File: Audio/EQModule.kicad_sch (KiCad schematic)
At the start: 59 parts, among them J6 AUX_IN, J7 V_IN, J8 AUX_OUT, U2 NJM4558, U3 NJM4558, U4 NJM4558

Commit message: AudioCaseのリレー・EQネット整理と分割Gerberを再生成する。
Controllでアンプ別リレーネットを分離し、EQのバッファ入力をL/R_BUFF_INに改名。4枚分割PCBと発注用Gerberを更新し、RVパネルKiKit矩形とmacOS向けツール探索も修正。

Co-authored-by: Cursor <cursoragent@cursor.com>
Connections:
- net L_IN: no longer C20.1, C21.1, R16.1, U2.3 (+)
- net R_IN: no longer C18.1, C19.1, R15.1, U2.5 (+)
- new net L_BUFF_IN: C20.1, C21.1, R16.1, U2.3 (+)
- new net R_BUFF_IN: C18.1, C19.1, R15.1, U2.5 (+)
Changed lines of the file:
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@@
 		)
 	)
-	(label "L_IN"
+	(label "L_BUFF_IN"
 		(at 97.79 104.14 180)
 		(effects
@@
 		)
 	)
-	(label "R_IN"
+	(label "R_BUFF_IN"
 		(at 119.38 50.8 0)
 		(effects
@@
 		)
 	)
-	(label "L_IN"
+	(label "L_BUFF_IN"
 		(at 119.38 73.66 0)
 		(effects
@@
 		)
 	)
-	(label "R_IN"
+	(label "R_BUFF_IN"
 		(at 97.79 128.27 180)
 		(effects

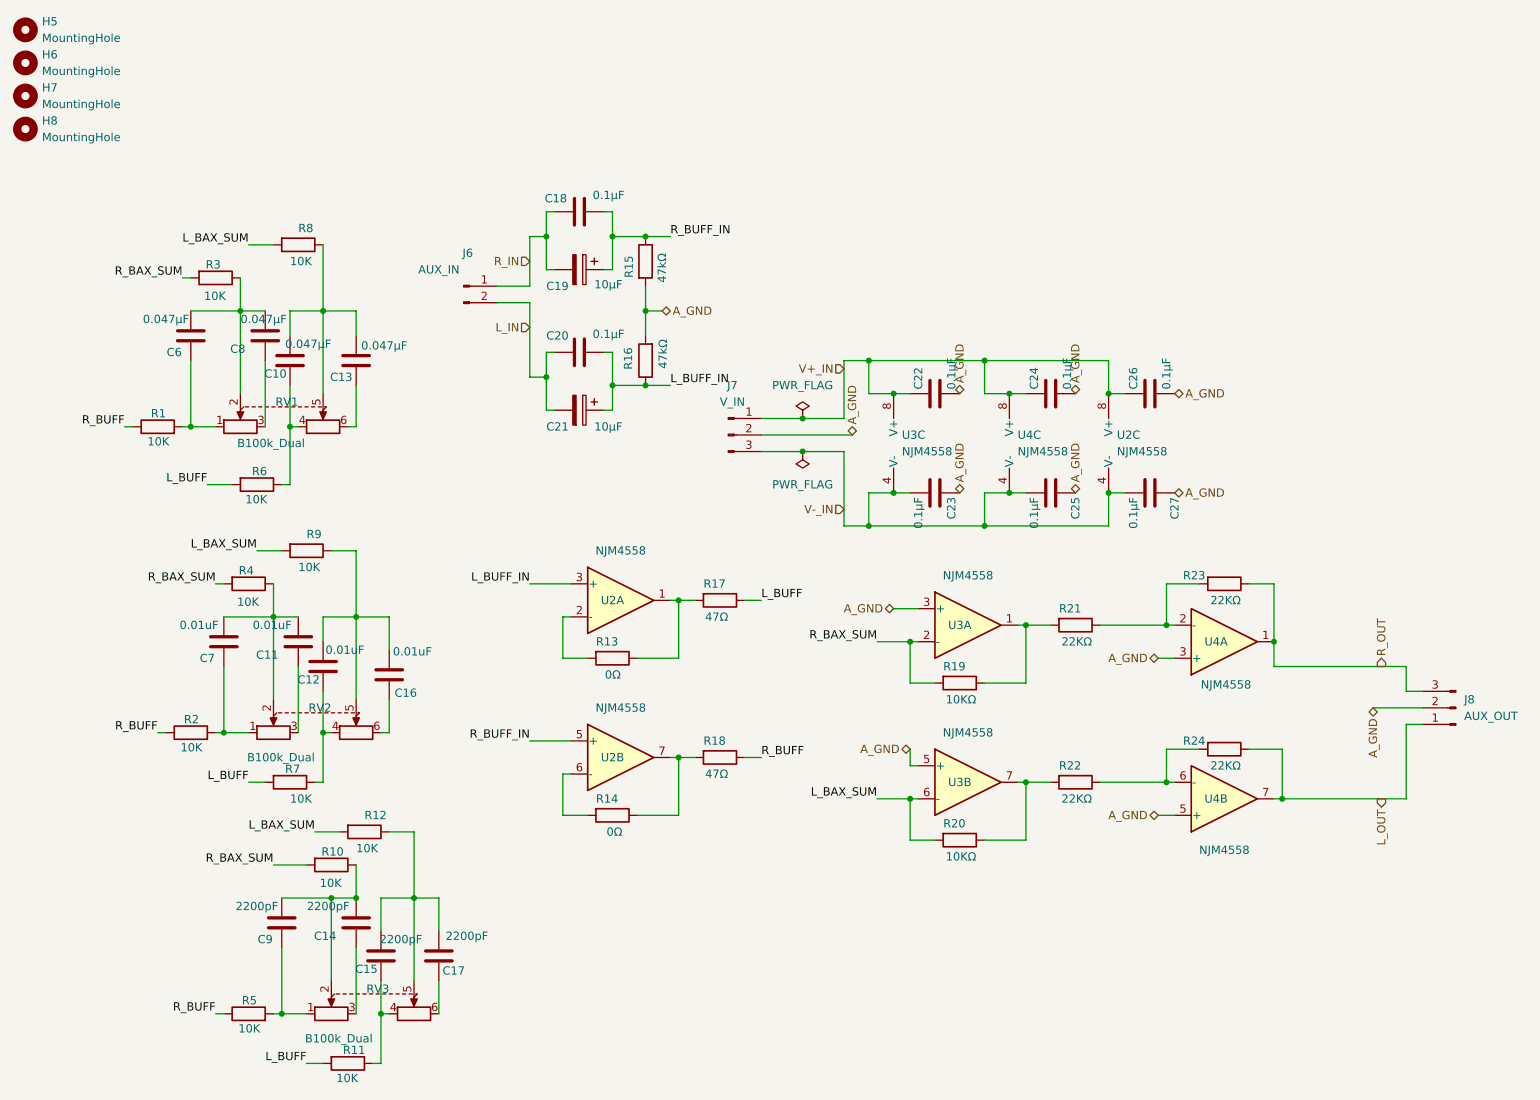
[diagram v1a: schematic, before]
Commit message: RVConvert基板を追加し、分割Gerber生成を5基板対応にする。
Co-authored-by: Cursor <cursoragent@cursor.com>
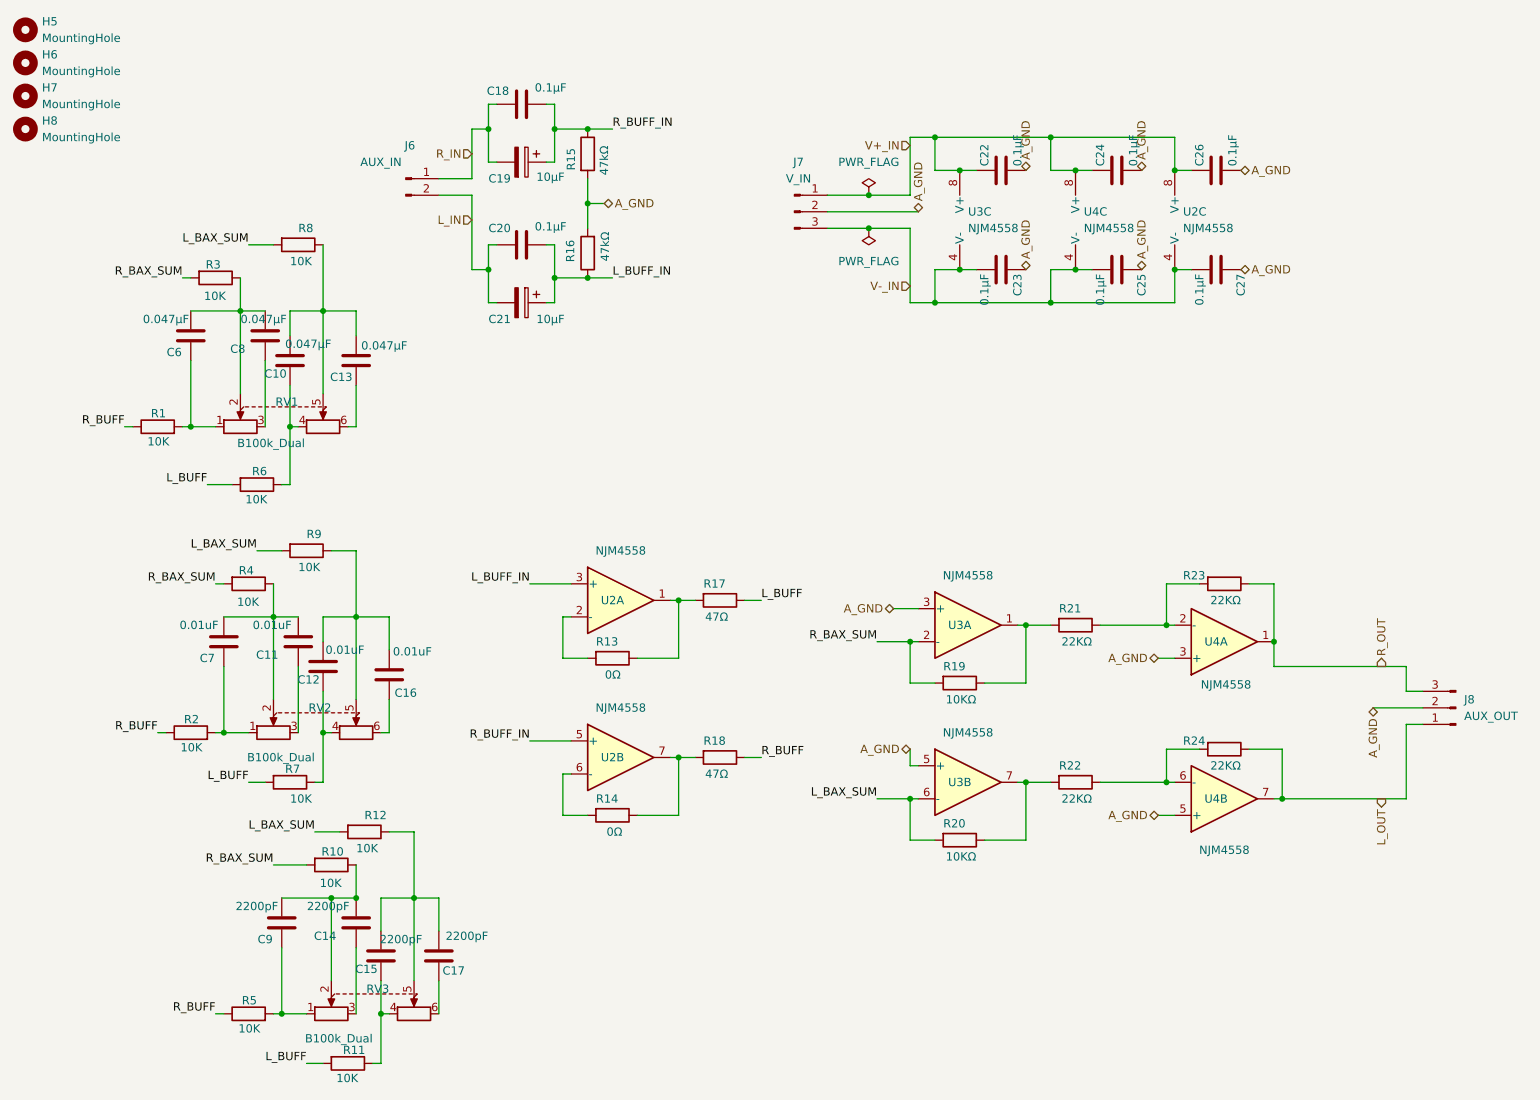
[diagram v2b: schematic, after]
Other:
- moved on the sheet: C18, C19, C20, C21, C22, C23, C24, C25, C26, C27, J6, J7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
